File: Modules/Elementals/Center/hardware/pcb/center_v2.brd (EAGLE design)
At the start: 17.8 x 100 mm, 24 parts, among them J1 WQP-PJ398SM6, J10 WQP-PJ398SM6, J11 WQP-PJ398SM6, J12 WQP-PJ398SM6, J2 WQP-PJ398SM6, J3 WQP-PJ398SM6, J4 WQP-PJ398SM6, J5 WQP-PJ398SM6, J6 WQP-PJ398SM6, J7 WQP-PJ398SM6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

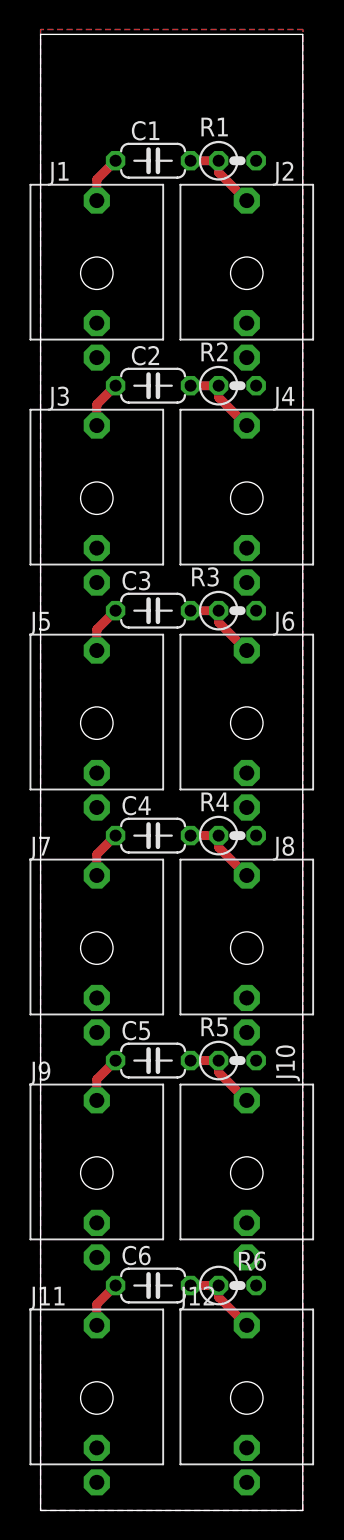
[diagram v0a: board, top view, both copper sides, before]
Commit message: Updated Elemental Center with more compact parts
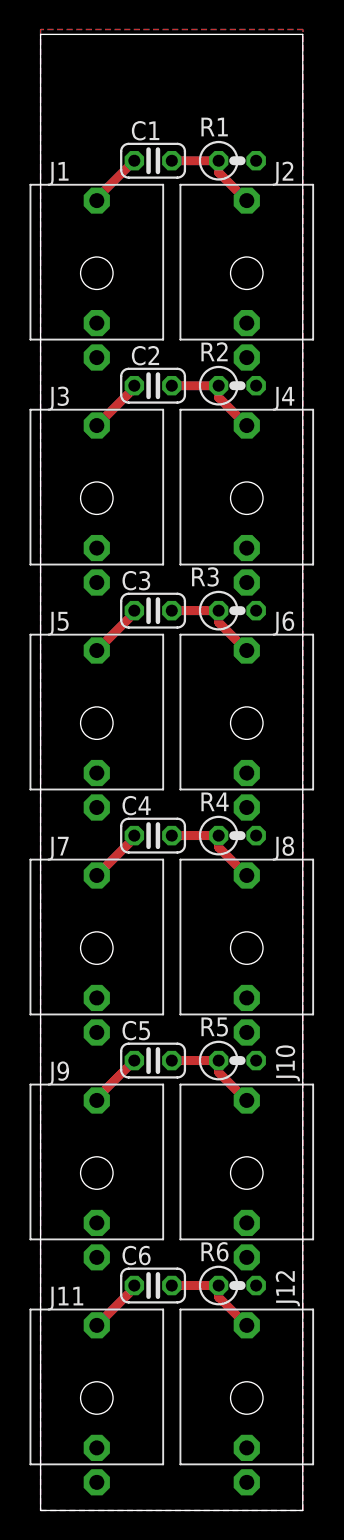
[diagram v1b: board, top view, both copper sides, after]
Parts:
- C1, C2, C3, C4, C5, C6: device SonicAthame:C050-024X044 -> SonicAthame:C025-024X044
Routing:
- net N$8: track 5.39 -> 6.66 mm
- net N$5: track 5.39 -> 6.66 mm
- net N$3: track 5.39 -> 6.66 mm
- net N$2: track 5.39 -> 6.66 mm
- net N$11: track 5.39 -> 6.66 mm
- net N$10: track 5.39 -> 6.66 mm
- net N$6: track 3.23 -> 3.75 mm
- net N$1: track 3.23 -> 3.75 mm
- net N$9: track 3.23 -> 3.75 mm
- net N$12: track 3.23 -> 3.75 mm
- net N$7: track 3.23 -> 3.75 mm
- net N$4: track 3.23 -> 3.75 mm
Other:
- board text added: "Sonic Athame is fully open-hardware and open-software! Find schematics and code on the official GitHub: github.com/nimaid/Sonic-Athame-eurorack"
- board text removed: "Sonic Athame is fully open-hardware and open-software!! Find schematics and code on the official GitHub: https://github.com/nimaid/Sonic-Athame-eurorack"
